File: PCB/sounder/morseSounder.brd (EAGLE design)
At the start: 56.6 x 82.7 mm, 77 parts, among them J1 AVR_SPI_PRG_6PTH, J2 POWERPOLE_POWER25A_HORIZONTAL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, J3 POWER_JACKPTH, U1 ATMEGA328P_TQFP

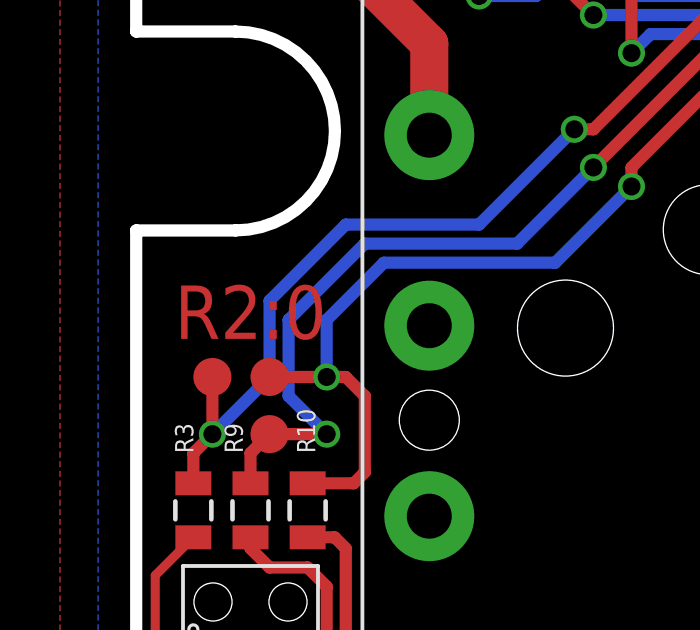
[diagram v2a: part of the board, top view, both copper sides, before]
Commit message: bumped version number on boards and updated panel 1 with new design
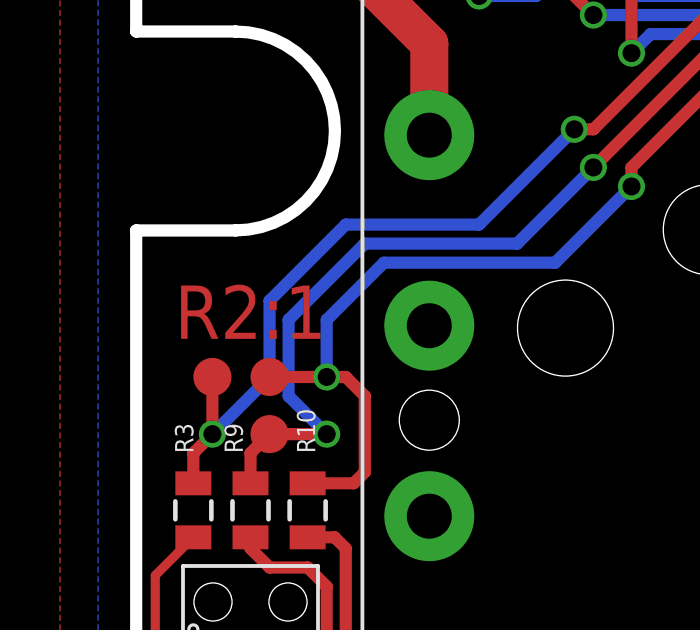
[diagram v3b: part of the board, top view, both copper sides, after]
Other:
- board text added: "R2:1"
- board text removed: "R2:0"
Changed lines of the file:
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@@
 <layer number="27" name="tValues" color="7" fill="1" visible="no" active="yes"/>
 <layer number="28" name="bValues" color="7" fill="1" visible="no" active="yes"/>
-<layer number="29" name="tStop" color="7" fill="3" visible="no" active="yes"/>
+<layer number="29" name="tStop" color="7" fill="3" visible="yes" active="yes"/>
 <layer number="30" name="bStop" color="7" fill="6" visible="no" active="yes"/>
 <layer number="31" name="tCream" color="7" fill="4" visible="no" active="yes"/>
@@
 <text x="7.62" y="77.47" size="1.27" layer="21" font="vector" align="center">Paddle/Key</text>
 <text x="28.448" y="35.56" size="1.778" layer="26" font="vector" rot="MR0" align="bottom-center">www.SUWS.org.uk</text>
-<text x="3.81" y="13.97" size="1.778" layer="1" font="vector" align="bottom-center">R2:0</text>
-<text x="3.81" y="13.97" size="1.778" layer="29" font="vector" align="bottom-center">R2:0</text>
+<text x="3.81" y="13.97" size="1.778" layer="1" font="vector" align="bottom-center">R2:1</text>
+<text x="3.81" y="13.97" size="1.778" layer="29" font="vector" align="bottom-center">R2:1</text>
 </plain>
 <attributes>

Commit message: Flip weight and rate controls to match front pannel
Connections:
- net ADC_RATE: now also TP2.P$1, U$6.R2, U1.23; no longer TP1.P$1, U$6.F2, U1.24
- net ADC_WEIGHT: now also TP1.P$1, U$6.F2, U1.24; no longer TP2.P$1, U$6.R2, U1.23
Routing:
- net ADC_WEIGHT: track 81.0 -> 74.8 mm
- net ADC_RATE: track 74.8 -> 81.0 mm
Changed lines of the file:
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@@
 <wire x1="50.26" y1="8.3" x2="50.165" y2="8.255" width="0" layer="19" extent="16-16"/>
 </signal>
-<signal name="ADC_RATE">
+<signal name="ADC_WEIGHT">
 <contactref element="U$6" pad="F2"/>
 <contactref element="TP1" pad="P$1"/>
@@
 <wire x1="46.98" y1="5.08" x2="48.26" y2="3.8" width="0.4064" layer="16"/>
 </signal>
-<signal name="ADC_WEIGHT">
+<signal name="ADC_RATE">
 <contactref element="U$6" pad="R2"/>
 <contactref element="TP2" pad="P$1"/>
